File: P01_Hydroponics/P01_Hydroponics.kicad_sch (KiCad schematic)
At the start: 1 part

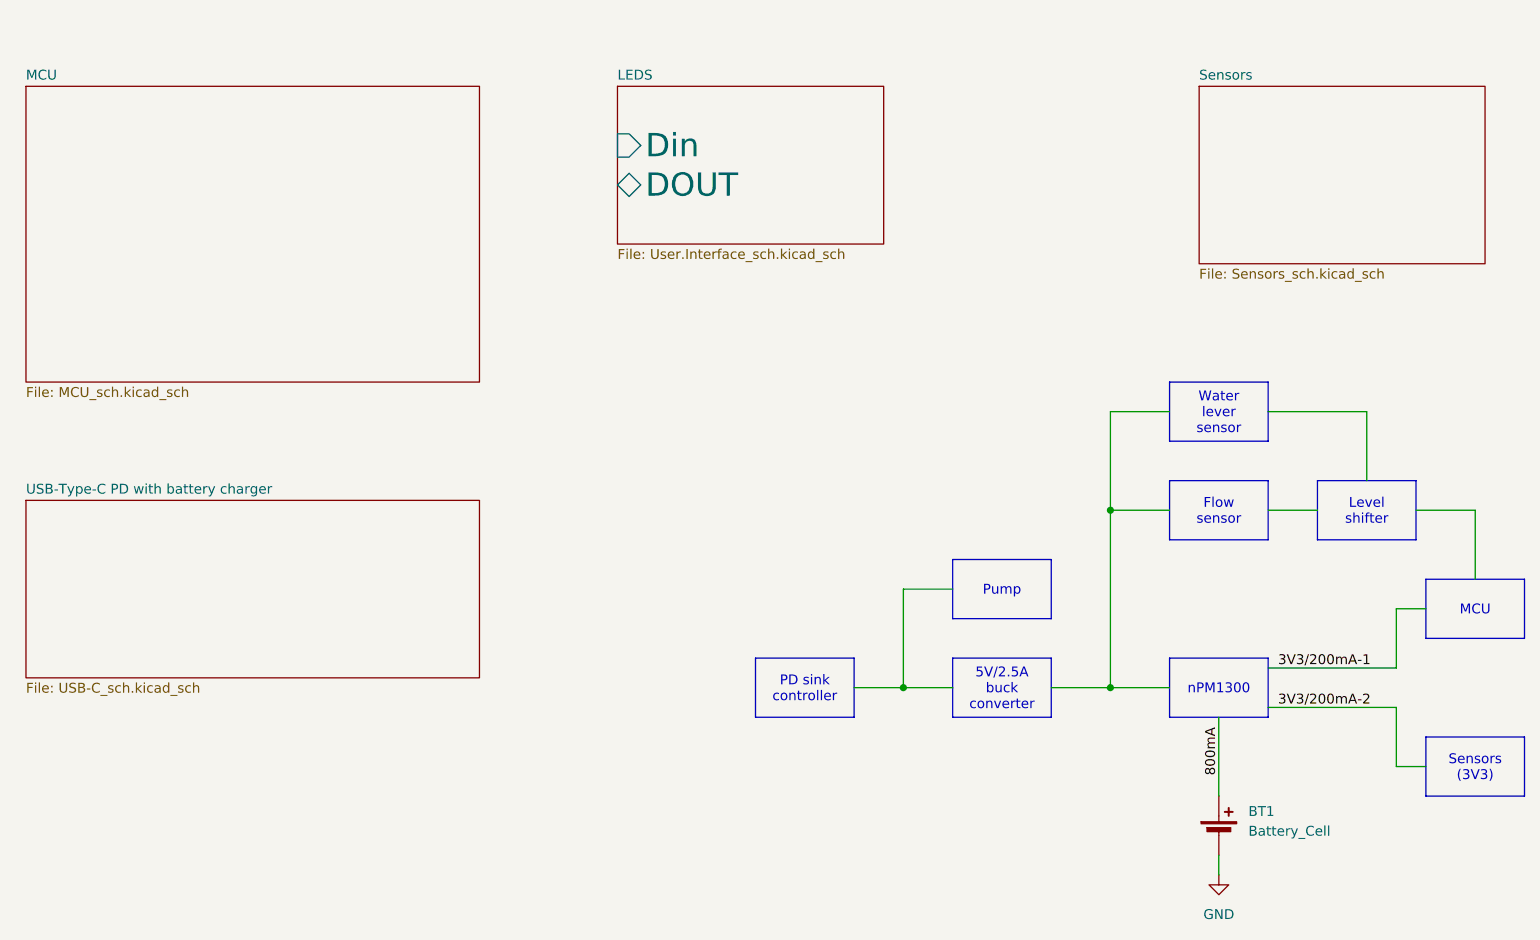
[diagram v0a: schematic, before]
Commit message: New version
Modified PD sink controller, and added 3v3 and 5V DC-DC buck converters
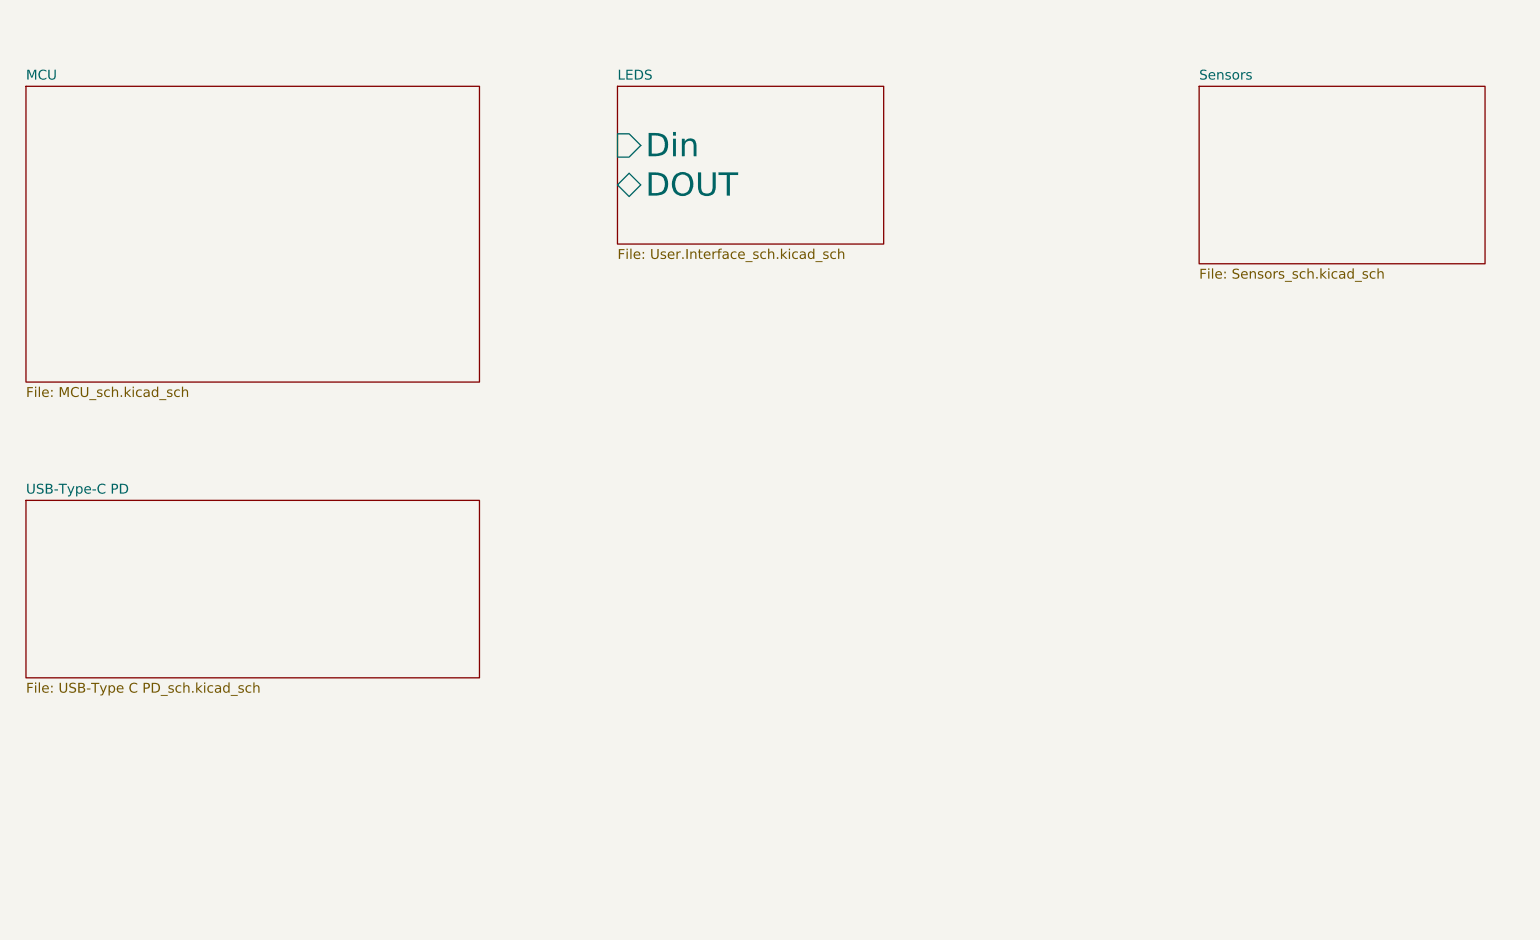
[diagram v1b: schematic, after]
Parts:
- removed BT1: Battery_Cell, symbol Device:Battery_Cell
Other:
- sheet USB-Type-C PD with battery charger renamed USB-Type-C PD
- sheet USB-Type-C PD: file USB-C_sch.kicad_sch -> USB-Type C PD_sch.kicad_sch

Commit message: Retry
bla bla
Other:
- added sheet Power (untitled.kicad_sch)
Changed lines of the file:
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@@
 	)
 	(sheet
-		(at 96.52 26.67)
+		(at 67.31 49.53)
+		(size 43.18 26.67)
+		(fields_autoplaced yes)
+		(stroke
+			(width 0.1524)
+			(type solid)
+		)
+		(fill
+			(color 0 0 0 0.0000)
+		)
+		(property "Sheetname" "Power"
+			(at 67.31 48.8184 0)
+			(effects
+				(font
+					(size 1.27 1.27)
+				)
+				(justify left bottom)
+			)
+		)
+		(property "Sheetfile" "untitled.kicad_sch"
+			(at 67.31 76.7846 0)
+			(effects
+				(font
+					(size 1.27 1.27)
+				)
+				(justify left top)
+			)
+		)
+		(instances
+			(project "P01_Hydroponics"
+				(path "/f251d969-db3d-42b0-b168-8992c4b2bbf4"
+					(page "6")
+				)
+			)
+		)
+	)
+	(sheet
+		(at 67.31 20.32)
 		(size 34.29 20.32)
 		(fields_autoplaced yes)
@@
 		)
 		(property "Sheetname" "LEDS"
-			(at 96.52 25.9584 0)
+			(at 67.31 19.6084 0)
 			(effects
 				(font
@@
 		)
 		(property "Sheetfile" "User.Interface_sch.kicad_sch"
-			(at 96.52 47.5746 0)
+			(at 67.31 41.2246 0)
 			(effects
 				(font
@@
 		)
 		(pin "Din" input
-			(at 96.52 34.29 180)
+			(at 67.31 27.94 180)
 			(effects
 				(font
@@
 		)
 		(pin "DOUT" tri_state
-			(at 96.52 39.37 180)
+			(at 67.31 33.02 180)
 			(effects
 				(font
@@
 	)
 	(sheet
-		(at 20.32 26.67)
-		(size 58.42 38.1)
+		(at 19.05 44.45)
+		(size 27.94 16.51)
 		(fields_autoplaced yes)
 		(stroke
@@
 		)
 		(property "Sheetname" "MCU"
-			(at 20.32 25.9584 0)
+			(at 19.05 43.7384 0)
 			(effects
 				(font
@@
 		)
 		(property "Sheetfile" "MCU_sch.kicad_sch"
-			(at 20.32 65.3546 0)
+			(at 19.05 61.5446 0)
 			(effects
 				(font
@@
 	)
 	(sheet
-		(at 20.32 80.01)
-		(size 58.42 22.86)
+		(at 19.05 21.59)
+		(size 27.94 15.24)
 		(fields_autoplaced yes)
 		(stroke
@@
 		)
 		(property "Sheetname" "USB-Type-C PD"
-			(at 20.32 79.2984 0)
+			(at 19.05 20.8784 0)
 			(effects
 				(font
@@
 		)
 		(property "Sheetfile" "USB-Type C PD_sch.kicad_sch"
-			(at 20.32 103.4546 0)
+			(at 19.05 37.4146 0)
 			(effects
 				(font
